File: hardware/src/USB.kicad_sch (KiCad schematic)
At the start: 25 parts, among them J301 USB_C_Receptacle_USB2.0_16P, Q301 NPN, Q302 NPN, U301 CP2102N-Axx-xQFN24

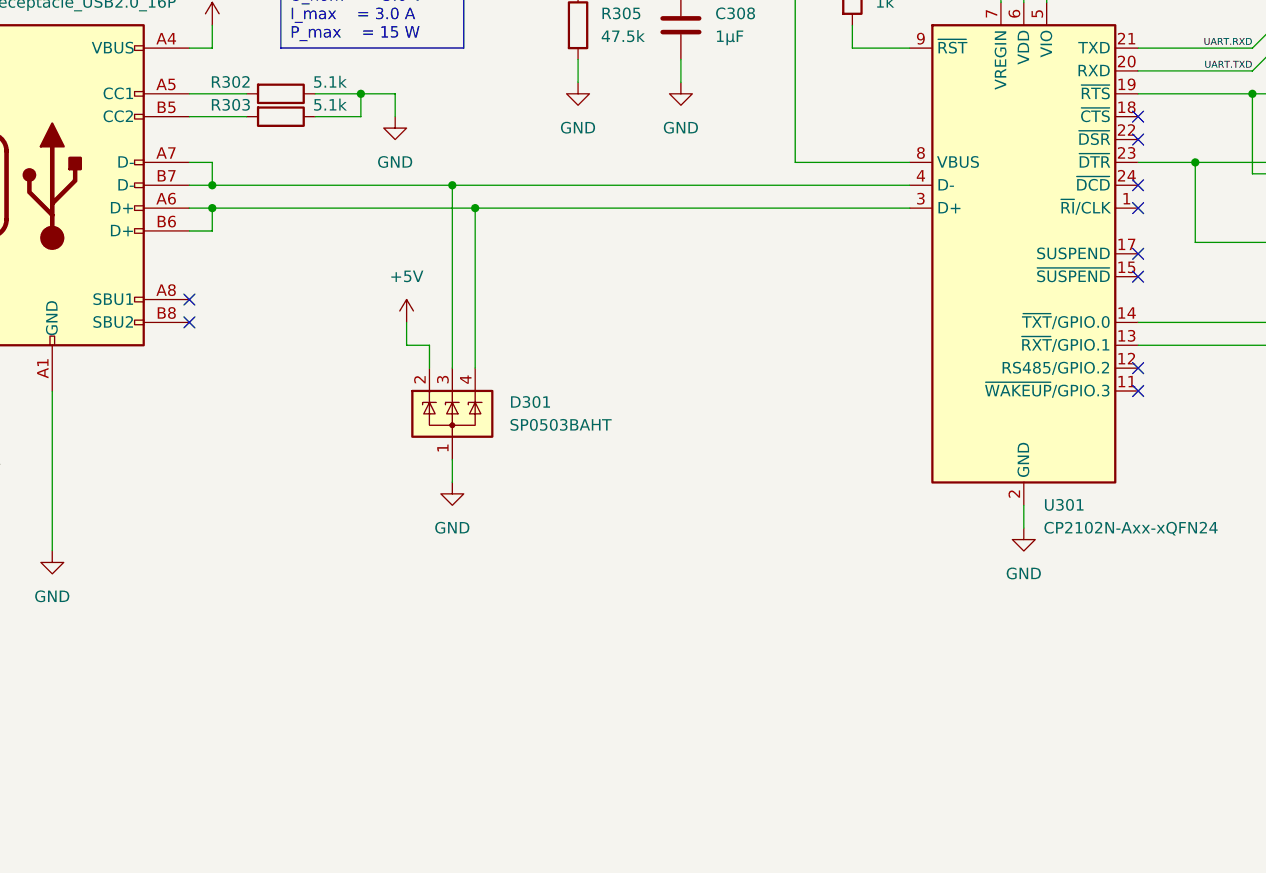
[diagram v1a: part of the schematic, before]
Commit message: Add: Alternative USB connection, directly to the ESP USB_DP and USB_DN
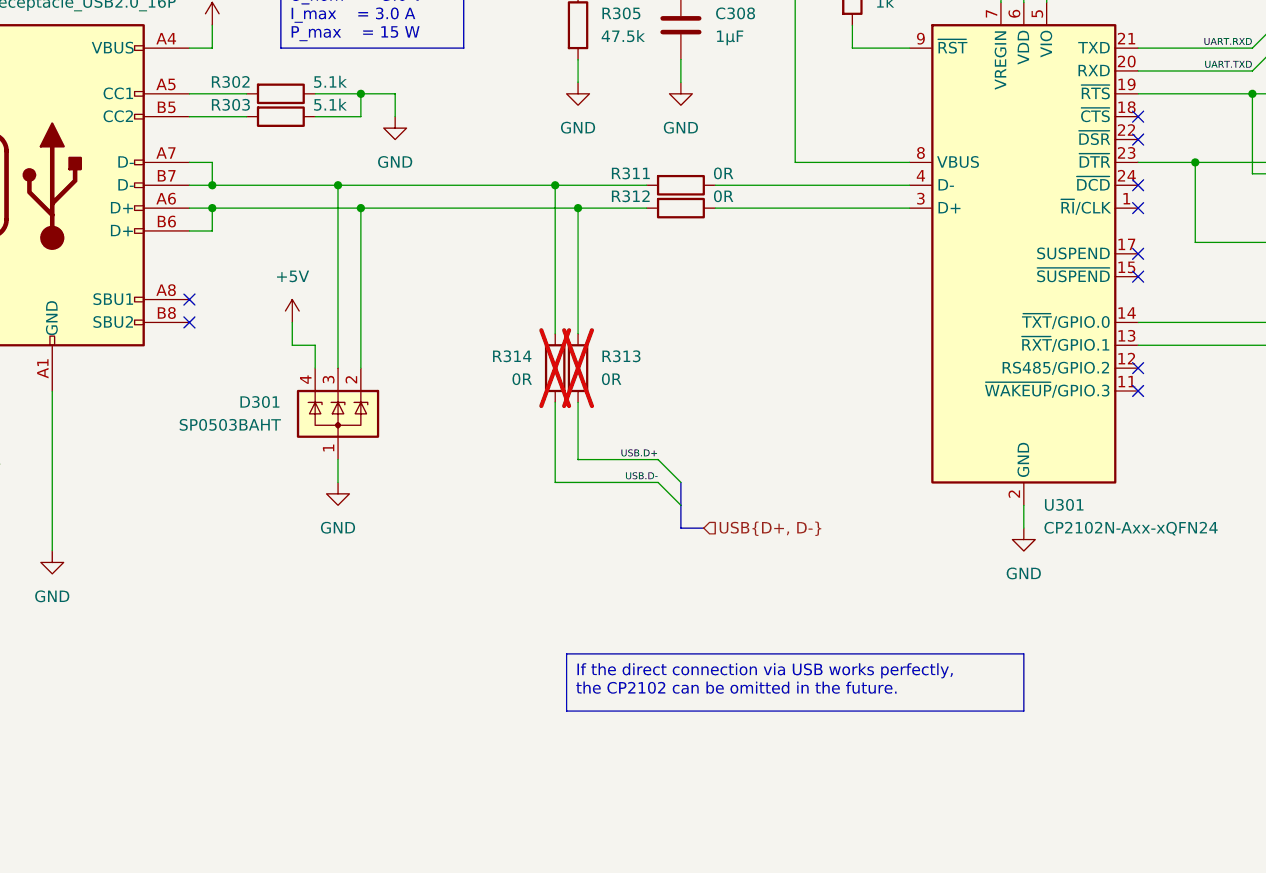
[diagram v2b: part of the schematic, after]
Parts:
- added R311, R312, R313, R314: 0R, symbol Device:R
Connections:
- net +5V: now also D301.4 (K); no longer D301.2 (K)
- net at J301.A6 (D+), J301.B6 (D+): now also D301.2 (K), R312.2, R313.1; no longer D301.4 (K), U301.3 (D+)
- net at D301.3 (K), J301.A7 (D-), J301.B7 (D-): now also R311.2, R314.1; no longer U301.4 (D-)
- new net: R312.1, U301.3 (D+)
- new net: R311.1, U301.4 (D-)
- new net USB.D+: R313.2
- new net USB.D-: R314.2
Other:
- moved on the sheet: D301
